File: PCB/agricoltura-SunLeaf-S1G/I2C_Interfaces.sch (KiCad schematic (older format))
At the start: 11 parts

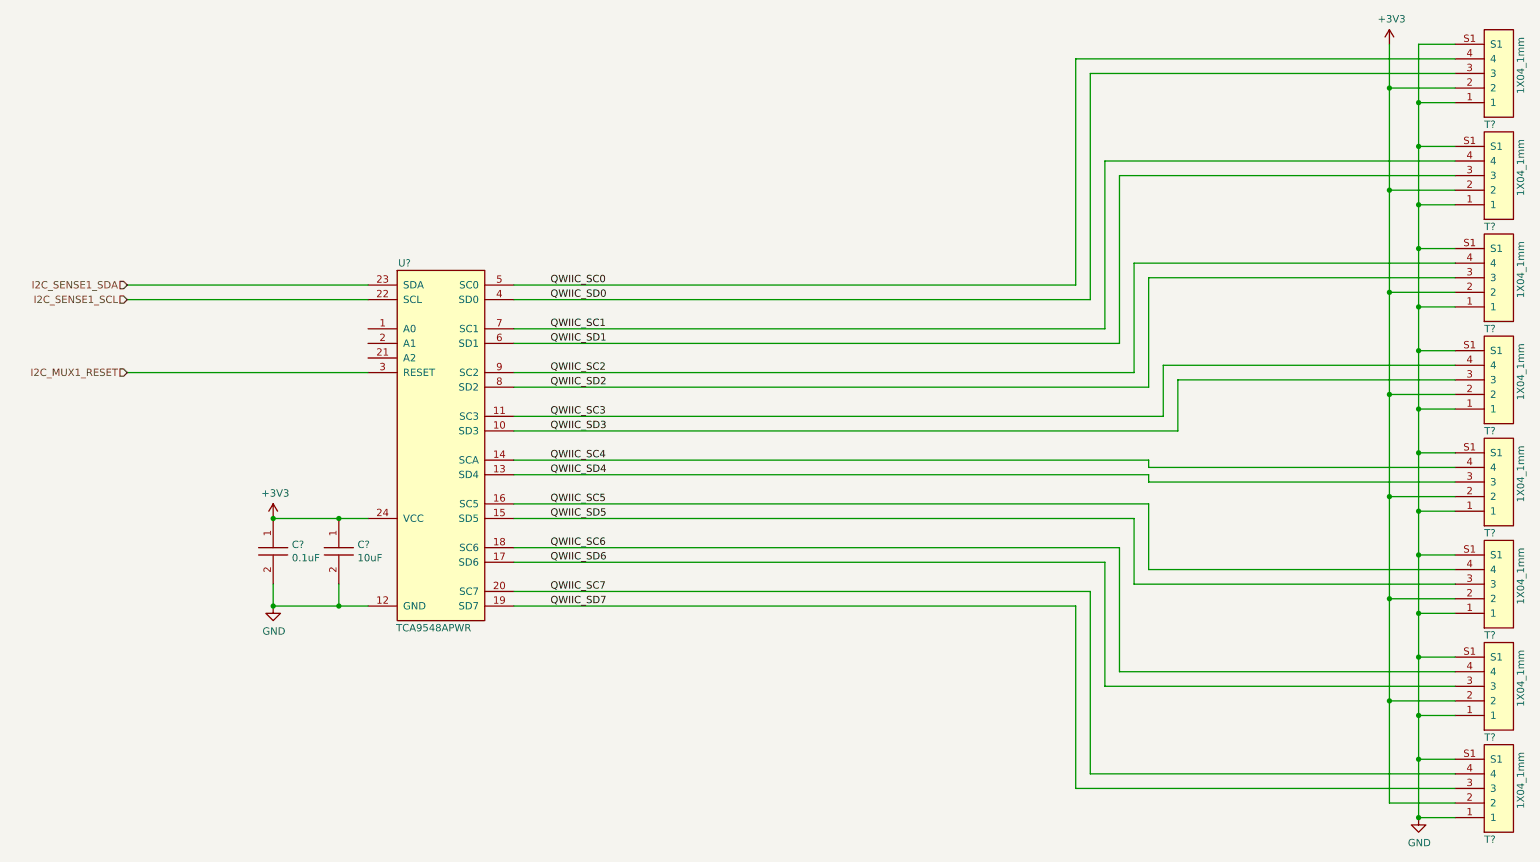
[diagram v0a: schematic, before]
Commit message: Schematic Complete
Schematic completed and PCB started
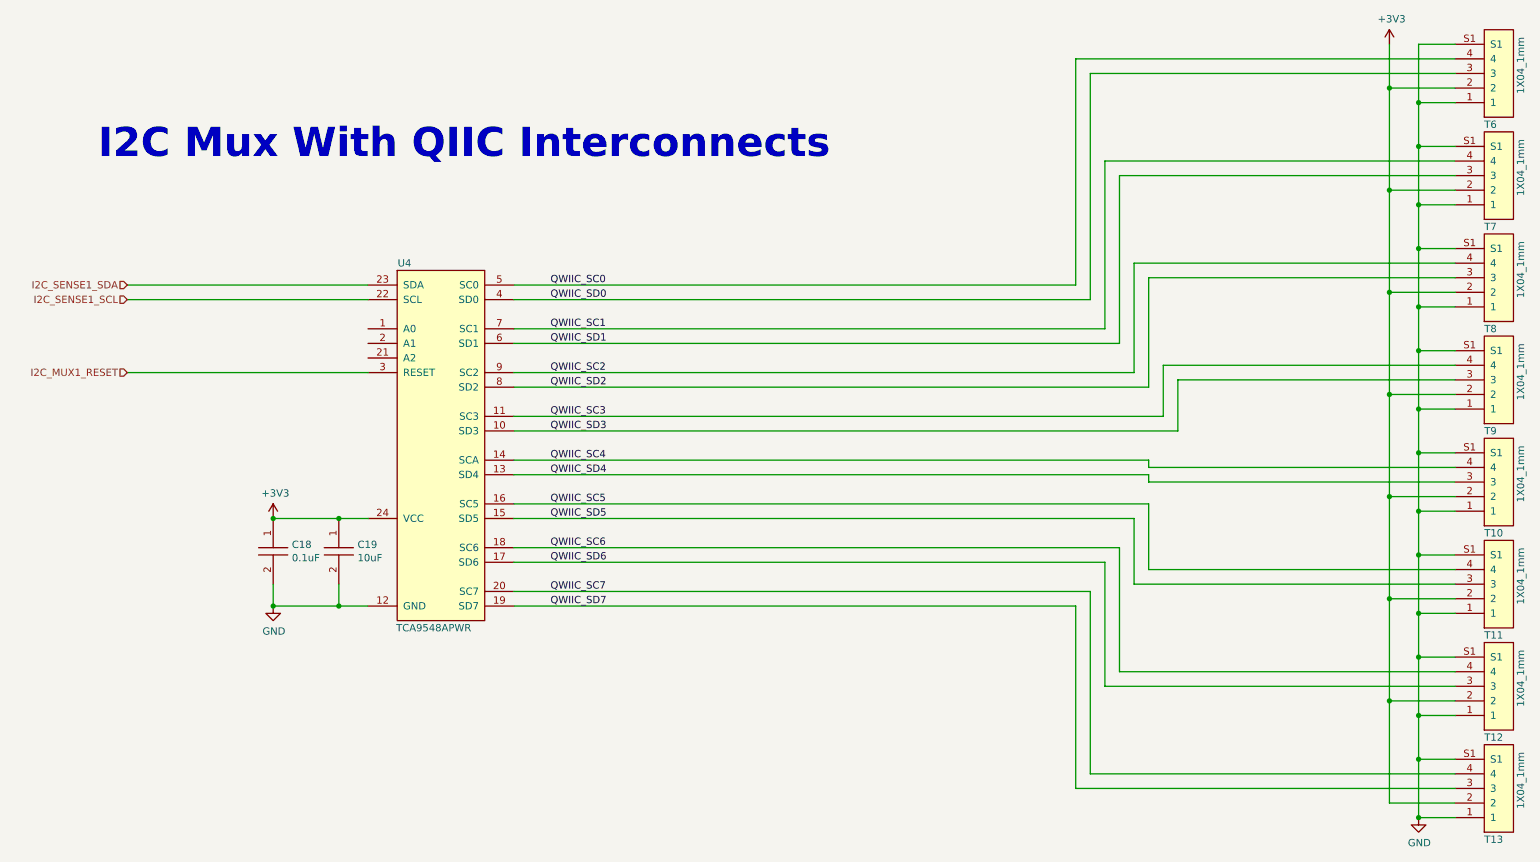
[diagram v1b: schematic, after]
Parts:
- gave numbers to parts that had none: 11
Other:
- note added: "I2C Mux With QIIC Interconnects"
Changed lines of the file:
@@
 AR Path="/5EE82896/5F11563E" Ref="C?"  Part="1"
 AR Path="/5EE827B2/5F11563E" Ref="C?"  Part="1"
-AR Path="/5F0552DA/5F11563E" Ref="C?"  Part="1"
-F 0 "C?" V 2879 4378 50  0000 L CNN
+AR Path="/5F0552DA/5F11563E" Ref="C19"  Part="1"
+F 0 "C19" V 2879 4378 50  0000 L CNN
 F 1 "GRM188R61A106KE69J" H 2950 4450 50  0001 C CNN
 F 2 "AVR-KiCAD-Lib-Capacitors:C0603" H 2700 4250 50  0001 C CNN
@@
 AR Path="/5EE82896/5F11561C" Ref="#PWR?"  Part="1"
 AR Path="/5EE827B2/5F11561C" Ref="#PWR?"  Part="1"
-AR Path="/5F0552DA/5F11561C" Ref="#PWR?"  Part="1"
-F 0 "#PWR?" H 2450 3900 50  0001 C CNN
+AR Path="/5F0552DA/5F11561C" Ref="#PWR029"  Part="1"
+F 0 "#PWR029" H 2450 3900 50  0001 C CNN
 F 1 "+3V3" H 2465 4223 50  0000 C CNN
 F 2 "" H 2450 4050 50  0001 C CNN
@@
 AR Path="/5EE82896/5F189177" Ref="#PWR?"  Part="1"
 AR Path="/5EE827B2/5F189177" Ref="#PWR?"  Part="1"
-AR Path="/5F0552DA/5F189177" Ref="#PWR?"  Part="1"
-F 0 "#PWR?" H 2450 4400 50  0001 C CNN
+AR Path="/5F0552DA/5F189177" Ref="#PWR030"  Part="1"
+F 0 "#PWR030" H 2450 4400 50  0001 C CNN
 F 1 "GND" H 2455 4477 50  0000 C CNN
 F 2 "" H 2450 4650 50  0001 C CNN
@@
 $EndComp
 $Comp
-L AVR-KiCAD-Lib-ICs:TCA9548APWR U?
+L AVR-KiCAD-Lib-ICs:TCA9548APWR U4
 U 1 1 5EF912D4
 P 3300 2350
-F 0 "U?" H 3350 2400 50  0000 C CNN
+F 0 "U4" H 3350 2400 50  0000 C CNN
 F 1 "TCA9548APWR" H 3350 2550 50  0001 C CNN
 F 2 "AVR-KiCAD-Lib-ICs:TCA9548APWR" H 5650 5050 50  0001 C CNN
@@
 AR Path="/5EE82702/5F0119BE" Ref="#PWR?"  Part="1"
 AR Path="/5EE827B2/5F0119BE" Ref="#PWR?"  Part="1"
-AR Path="/5F0552DA/5F0119BE" Ref="#PWR?"  Part="1"
-F 0 "#PWR?" H 10300 5850 50  0001 C CNN
+AR Path="/5F0552DA/5F0119BE" Ref="#PWR032"  Part="1"
+F 0 "#PWR032" H 10300 5850 50  0001 C CNN
 F 1 "GND" H 10305 5927 50  0000 C CNN
 F 2 "" H 10300 6100 50  0001 C CNN
@@
 AR Path="/5EE82896/5F11565D" Ref="C?"  Part="1"
 AR Path="/5EE827B2/5F11565D" Ref="C?"  Part="1"
-AR Path="/5F0552DA/5F11565D" Ref="C?"  Part="1"
-F 0 "C?" V 2429 4378 50  0000 L CNN
+AR Path="/5F0552DA/5F11565D" Ref="C18"  Part="1"
+F 0 "C18" V 2429 4378 50  0000 L CNN
 F 1 "C0402C104K9PACTU" H 2500 4450 50  0001 C CNN
 F 2 "AVR-KiCAD-Lib-Resistors:R0402" H 2250 4250 50  0001 C CNN
@@
 AR Path="/5EE82896/5F11A0D2" Ref="#PWR?"  Part="1"
 AR Path="/5EE827B2/5F11A0D2" Ref="#PWR?"  Part="1"
-AR Path="/5F0552DA/5F11A0D2" Ref="#PWR?"  Part="1"
-F 0 "#PWR?" H 10100 650 50  0001 C CNN
+AR Path="/5F0552DA/5F11A0D2" Ref="#PWR031"  Part="1"
+F 0 "#PWR031" H 10100 650 50  0001 C CNN
 F 1 "+3V3" H 10115 973 50  0000 C CNN
 F 2 "" H 10100 800 50  0001 C CNN
@@
 	10100 1800 10100 2500
 $Comp
-L AVR-KiCAD-Lib-Connectors:BM04B-SRSS-TB(LF)(SN) T?
+L AVR-KiCAD-Lib-Connectors:BM04B-SRSS-TB(LF)(SN) T6
 U 1 1 5EEEF4BF
 P 10750 1300
-F 0 "T?" H 10750 1350 50  0000 L CNN
+F 0 "T6" H 10750 1350 50  0000 L CNN
 F 1 "BM04B-SRSS-TB(LF)(SN)" H 10800 1500 50  0001 C CNN
 F 2 "AVR-KiCAD-Lib-Connectors:CONN_BM04B-SRSS-TB(LF)(SN)" H 9850 1900 50  0001 C CNN
@@
 $EndComp
 $Comp
-L AVR-KiCAD-Lib-Connectors:BM04B-SRSS-TB(LF)(SN) T?
+L AVR-KiCAD-Lib-Connectors:BM04B-SRSS-TB(LF)(SN) T7
 U 1 1 5EEF134A
 P 10750 2000
-F 0 "T?" H 10750 2050 50  0000 L CNN
+F 0 "T7" H 10750 2050 50  0000 L CNN
 F 1 "BM04B-SRSS-TB(LF)(SN)" H 10800 2200 50  0001 C CNN
 F 2 "AVR-KiCAD-Lib-Connectors:CONN_BM04B-SRSS-TB(LF)(SN)" H 9850 2600 50  0001 C CNN
@@
 $EndComp
 $Comp
-L AVR-KiCAD-Lib-Connectors:BM04B-SRSS-TB(LF)(SN) T?
+L AVR-KiCAD-Lib-Connectors:BM04B-SRSS-TB(LF)(SN) T8
 U 1 1 5EEF30FD
 P 10750 2700
-F 0 "T?" H 10750 2750 50  0000 L CNN
+F 0 "T8" H 10750 2750 50  0000 L CNN
 F 1 "BM04B-SRSS-TB(LF)(SN)" H 10800 2900 50  0001 C CNN
 F 2 "AVR-KiCAD-Lib-Connectors:CONN_BM04B-SRSS-TB(LF)(SN)" H 9850 3300 50  0001 C CNN
@@
 $EndComp
 $Comp
-L AVR-KiCAD-Lib-Connectors:BM04B-SRSS-TB(LF)(SN) T?
+L AVR-KiCAD-Lib-Connectors:BM04B-SRSS-TB(LF)(SN) T9
 U 1 1 5EEF62A4
 P 10750 3400
-F 0 "T?" H 10750 3450 50  0000 L CNN
+F 0 "T9" H 10750 3450 50  0000 L CNN
 F 1 "BM04B-SRSS-TB(LF)(SN)" H 10800 3600 50  0001 C CNN
 F 2 "AVR-KiCAD-Lib-Connectors:CONN_BM04B-SRSS-TB(LF)(SN)" H 9850 4000 50  0001 C CNN
@@
 $EndComp
 $Comp
-L AVR-KiCAD-Lib-Connectors:BM04B-SRSS-TB(LF)(SN) T?
+L AVR-KiCAD-Lib-Connectors:BM04B-SRSS-TB(LF)(SN) T10
 U 1 1 5EEF749B
 P 10750 4100
-F 0 "T?" H 10750 4150 50  0000 L CNN
+F 0 "T10" H 10750 4150 50  0000 L CNN
 F 1 "BM04B-SRSS-TB(LF)(SN)" H 10800 4300 50  0001 C CNN
 F 2 "AVR-KiCAD-Lib-Connectors:CONN_BM04B-SRSS-TB(LF)(SN)" H 9850 4700 50  0001 C CNN
@@
 $EndComp
 $Comp
-L AVR-KiCAD-Lib-Connectors:BM04B-SRSS-TB(LF)(SN) T?
+L AVR-KiCAD-Lib-Connectors:BM04B-SRSS-TB(LF)(SN) T11
 U 1 1 5EEF95E6
 P 10750 4800
-F 0 "T?" H 10750 4850 50  0000 L CNN
+F 0 "T11" H 10750 4850 50  0000 L CNN
 F 1 "BM04B-SRSS-TB(LF)(SN)" H 10800 5000 50  0001 C CNN
 F 2 "AVR-KiCAD-Lib-Connectors:CONN_BM04B-SRSS-TB(LF)(SN)" H 9850 5400 50  0001 C CNN
@@
 $EndComp
 $Comp
-L AVR-KiCAD-Lib-Connectors:BM04B-SRSS-TB(LF)(SN) T?
+L AVR-KiCAD-Lib-Connectors:BM04B-SRSS-TB(LF)(SN) T12
 U 1 1 5EEFAAE5
 P 10750 5500
-F 0 "T?" H 10750 5550 50  0000 L CNN
+F 0 "T12" H 10750 5550 50  0000 L CNN
 F 1 "BM04B-SRSS-TB(LF)(SN)" H 10800 5700 50  0001 C CNN
 F 2 "AVR-KiCAD-Lib-Connectors:CONN_BM04B-SRSS-TB(LF)(SN)" H 9850 6100 50  0001 C CNN
@@
 $EndComp
 $Comp
-L AVR-KiCAD-Lib-Connectors:BM04B-SRSS-TB(LF)(SN) T?
+L AVR-KiCAD-Lib-Connectors:BM04B-SRSS-TB(LF)(SN) T13
 U 1 1 5EEFC790
 P 10750 6200
-F 0 "T?" H 10750 6250 50  0000 L CNN
+F 0 "T13" H 10750 6250 50  0000 L CNN
 F 1 "BM04B-SRSS-TB(LF)(SN)" H 10800 6400 50  0001 C CNN
 F 2 "AVR-KiCAD-Lib-Connectors:CONN_BM04B-SRSS-TB(LF)(SN)" H 9850 6800 50  0001 C CNN
@@
 Text HLabel 1450 3050 0    50   Input ~ 0
 I2C_MUX1_RESET
+Text Notes 1250 1600 0    200  ~ 40
+I2C Mux With QIIC Interconnects
 $EndSCHEMATC

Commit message: PCB Progress
added TVS diodes fo QWIIC connector serial signals. Did more routing overall.
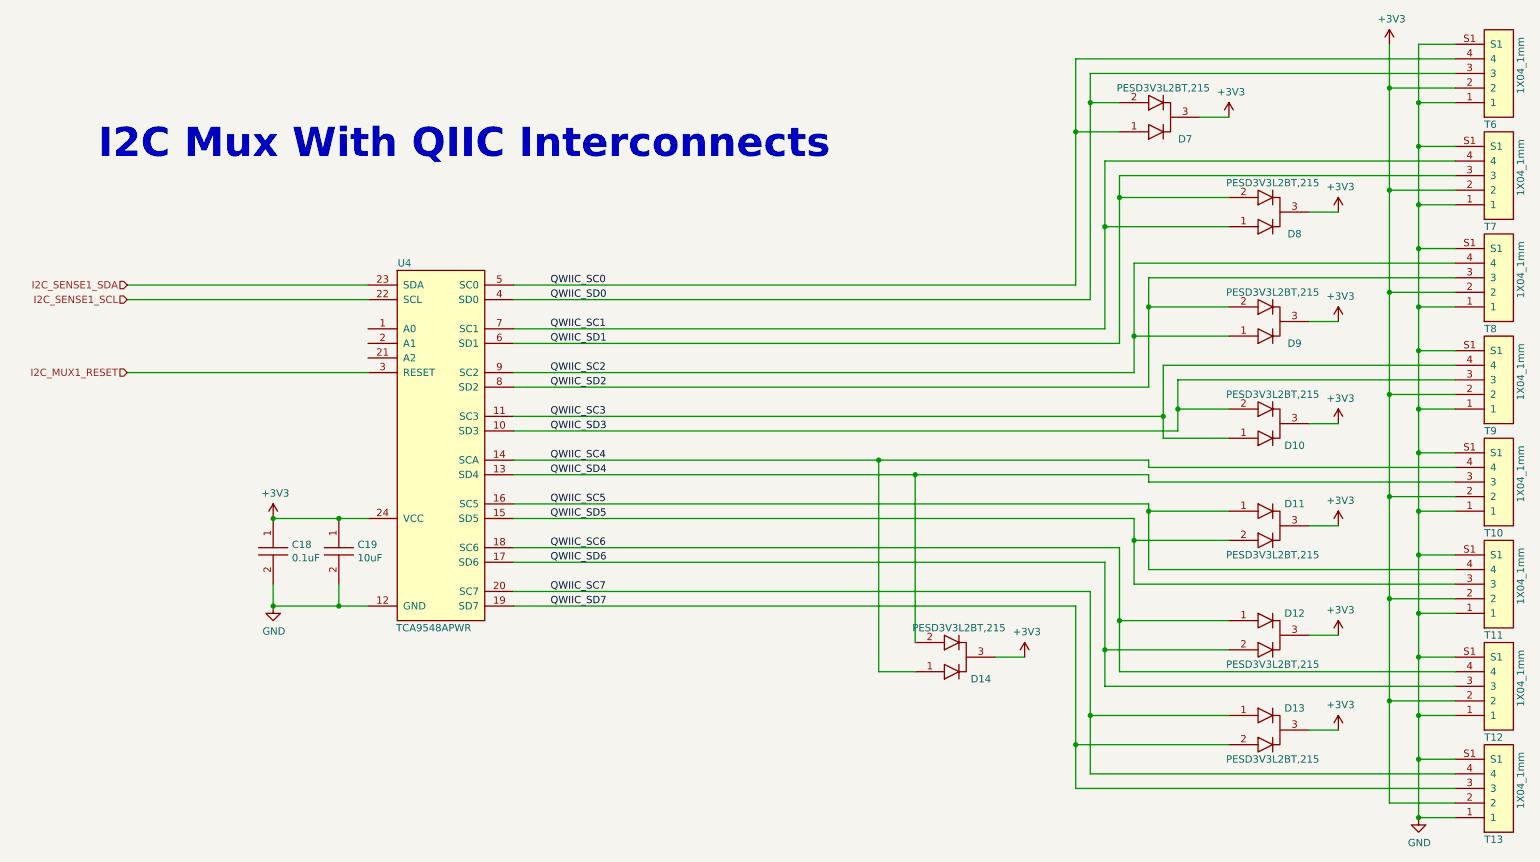
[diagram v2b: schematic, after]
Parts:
- added D10, D11, D12, D13, D14, D7, D8, D9: PESD3V3L2BT,215, AVR-KiCAD-Lib-Diodes:SOT-23, symbol AVR-KiCAD-Lib-Diodes:PESD3V3L2BT,215
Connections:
- net +3V3: now also D10.3, D11.3, D12.3, D13.3, D14.3, D7.3, D8.3, D9.3
- net QWIIC_SC0: now also D7.1
- net QWIIC_SC1: now also D8.1
- net QWIIC_SC2: now also D9.1
- net QWIIC_SC3: now also D10.1
- net QWIIC_SC4: now also D14.1
- net QWIIC_SC5: now also D11.1
- net QWIIC_SC6: now also D12.1
- net QWIIC_SC7: now also D13.1
- net QWIIC_SD0: now also D7.2
- net QWIIC_SD1: now also D8.2
- net QWIIC_SD2: now also D9.2
- net QWIIC_SD3: now also D10.2
- net QWIIC_SD4: now also D14.2
- net QWIIC_SD5: now also D11.2
- net QWIIC_SD6: now also D12.2
- net QWIIC_SD7: now also D13.2

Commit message: Pullups
Added pullup reistors to I2C ports, changed JTAG connector over to Tag connect.
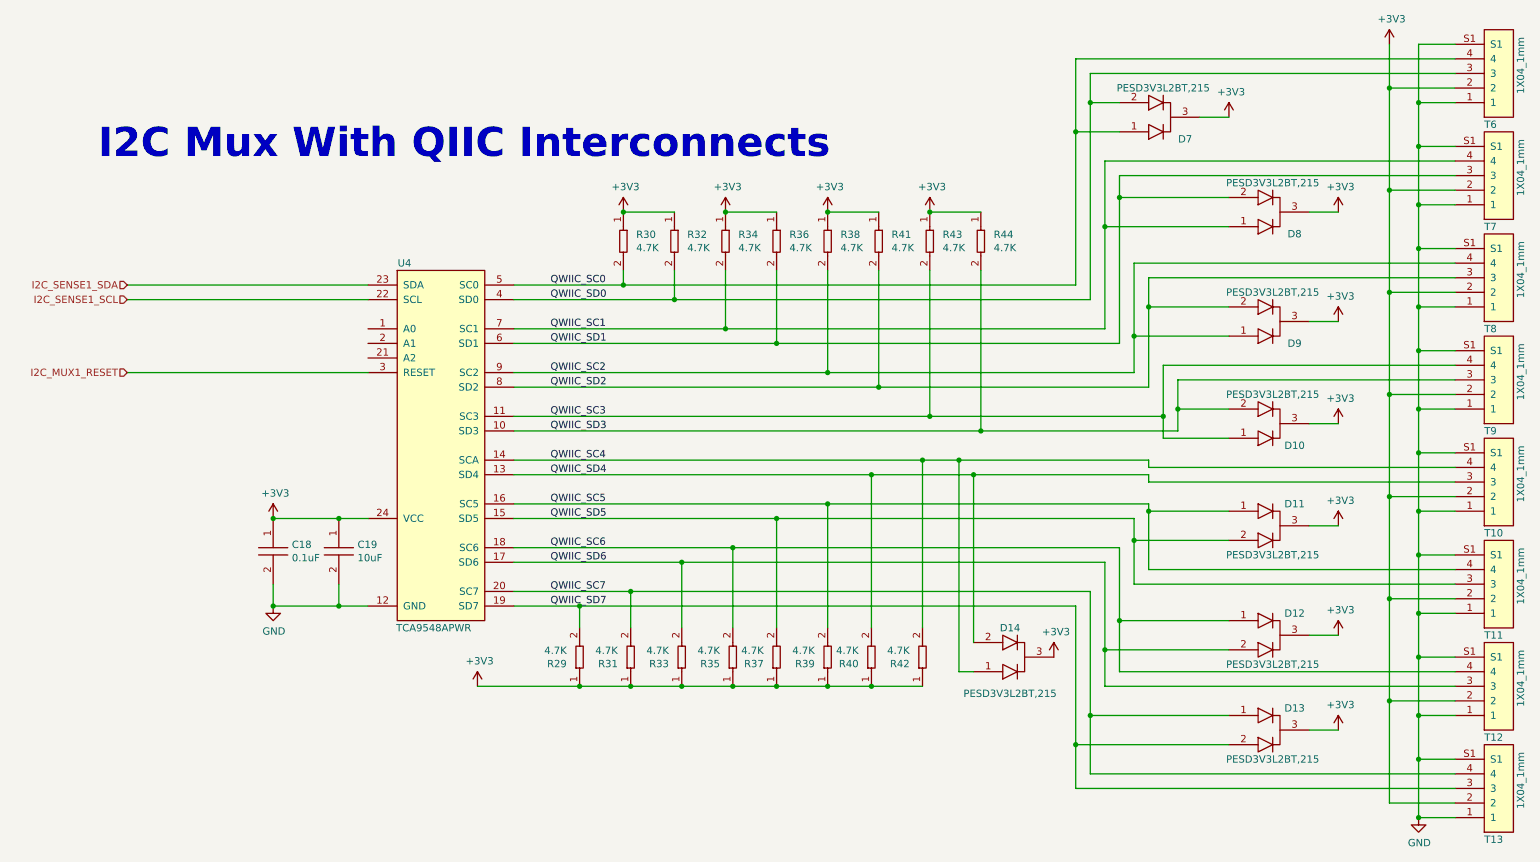
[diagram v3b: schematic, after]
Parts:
- added R29, R30, R31, R32, R33, R34, R35, R36, R37, R38, R39, R40, R41, R42, R43, R44: RC0402FR-074K7L, AVR-KiCAD-Lib-Resistors:R0402, symbol AVR-KiCAD-Lib-Resistors:RC0402FR-074K7L
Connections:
- net +3V3: now also R29.1, R30.1, R31.1, R32.1, R33.1, R34.1, R35.1, R36.1, R37.1, R38.1, R39.1, R40.1, R41.1, R42.1, R43.1, R44.1
- net QWIIC_SC0: now also R30.2
- net QWIIC_SC1: now also R34.2
- net QWIIC_SC2: now also R38.2
- net QWIIC_SC3: now also R43.2
- net QWIIC_SC4: now also R42.2
- net QWIIC_SC5: now also R39.2
- net QWIIC_SC6: now also R35.2
- net QWIIC_SC7: now also R31.2
- net QWIIC_SD0: now also R32.2
- net QWIIC_SD1: now also R36.2
- net QWIIC_SD2: now also R41.2
- net QWIIC_SD3: now also R44.2
- net QWIIC_SD4: now also R40.2
- net QWIIC_SD5: now also R37.2
- net QWIIC_SD6: now also R33.2
- net QWIIC_SD7: now also R29.2
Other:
- moved on the sheet: D14
